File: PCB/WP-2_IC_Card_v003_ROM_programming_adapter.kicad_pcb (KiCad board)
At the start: 2 copper layers, 19.7 x 49.5 mm, 2 parts, among them J1 Conn_01x38_Male, J2 Conn_02x16_Counter_Clockwise

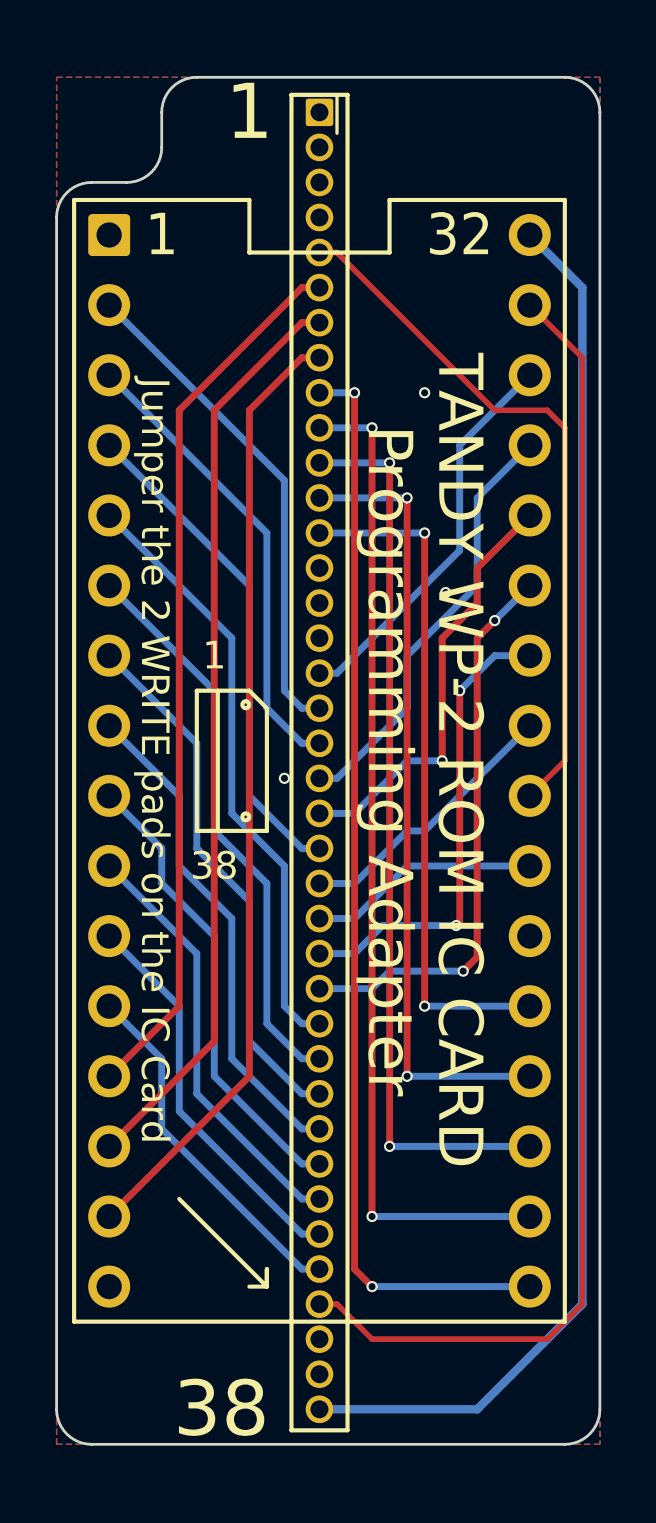
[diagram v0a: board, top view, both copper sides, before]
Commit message: reroute battery traces. cosmetics
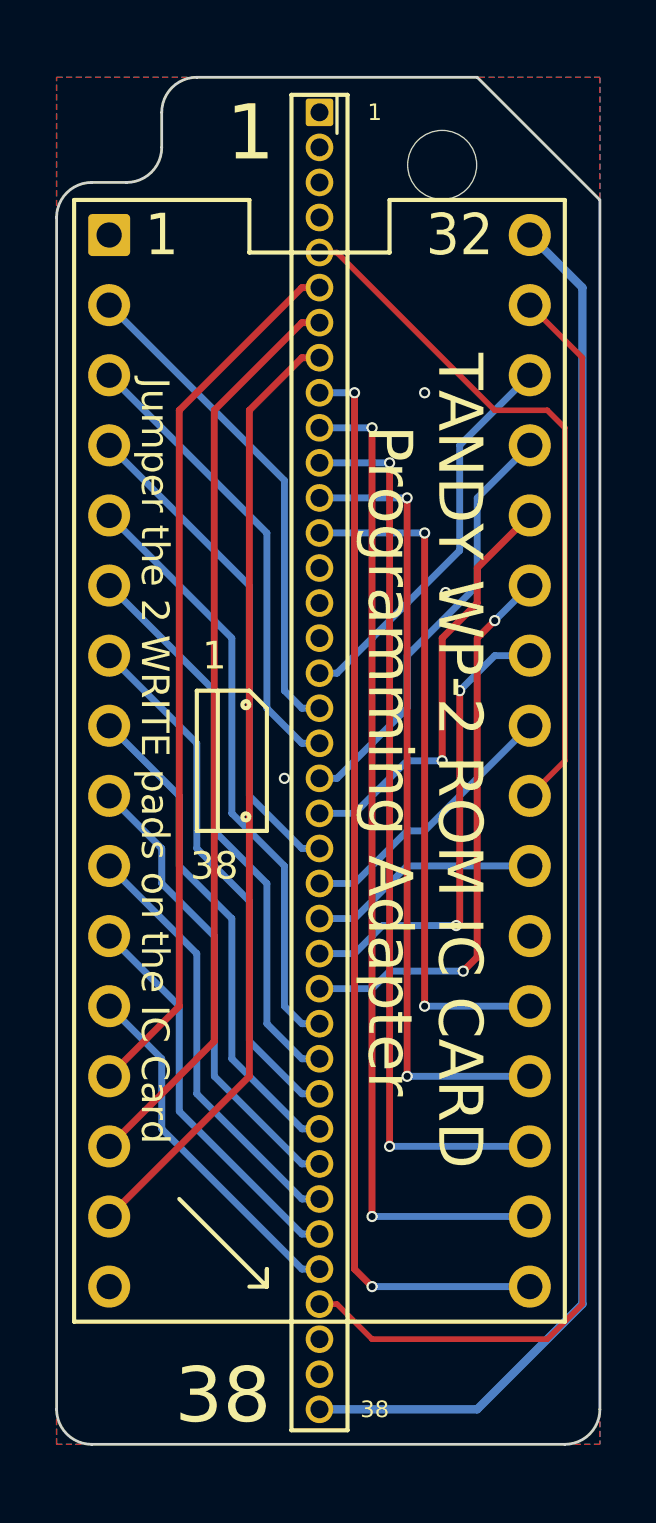
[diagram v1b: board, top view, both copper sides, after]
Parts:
- added REF**: MountingHole_2.5mm, MountingHole:MountingHole_2.5mm, F.Cu at (156.8, 80.0)
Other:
- outline, holes or cut-outs redrawn

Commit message: reduce programming adapter board size
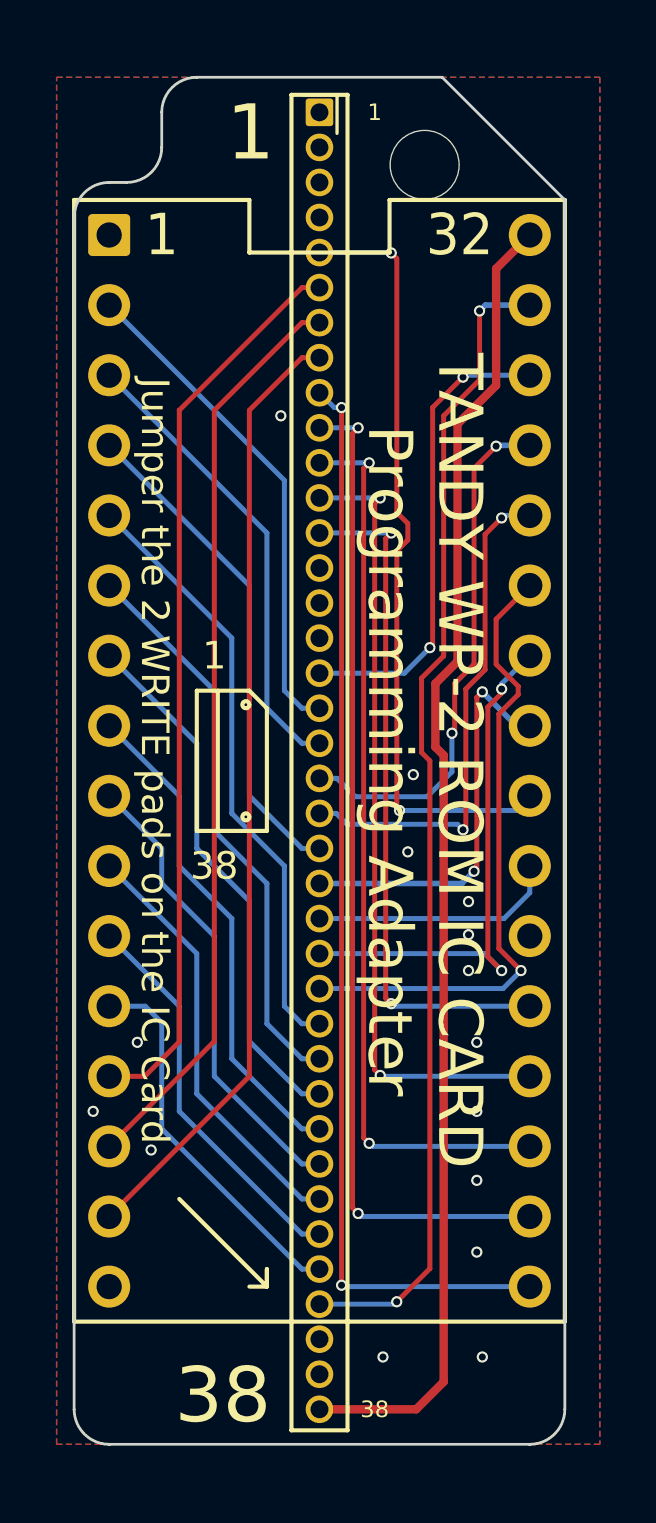
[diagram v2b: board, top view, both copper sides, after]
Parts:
- moved REF** 0.63 mm to (156.2, 80.0)
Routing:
- net /R~W: track 47.6 -> 42.1 mm, vias 0 -> 2
- net /A11: track 9.99 -> 15.3 mm, vias 0 -> 2
- net /A14: track 15.6 -> 19.1 mm, vias 0 -> 2
- net /A13: track 15.4 -> 18.4 mm, vias 1 -> 2
- net /A17: track 14.3 -> 17.2 mm, vias 0 -> 2
- net /~OE: track 25.4 -> 28.2 mm, vias 0 -> 2
- net /VDD: track 50.6 -> 48.0 mm
- net /A8: track 20.4 -> 23.0 mm, vias 2 -> 1
- net /A9: track 17.0 -> 19.1 mm
- net /A0: track 13.1 -> 13.8 mm
- net /D0: track 32.1 -> 32.9 mm
- net /A10: track 8.41 -> 8.98 mm
- net GND: vias 3 -> 15
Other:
- board size 19.7 x 49.5 mm -> 17.8 x 49.5 mm
- rule trace_min: 0.2 -> 0.16

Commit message: programming adapter routing
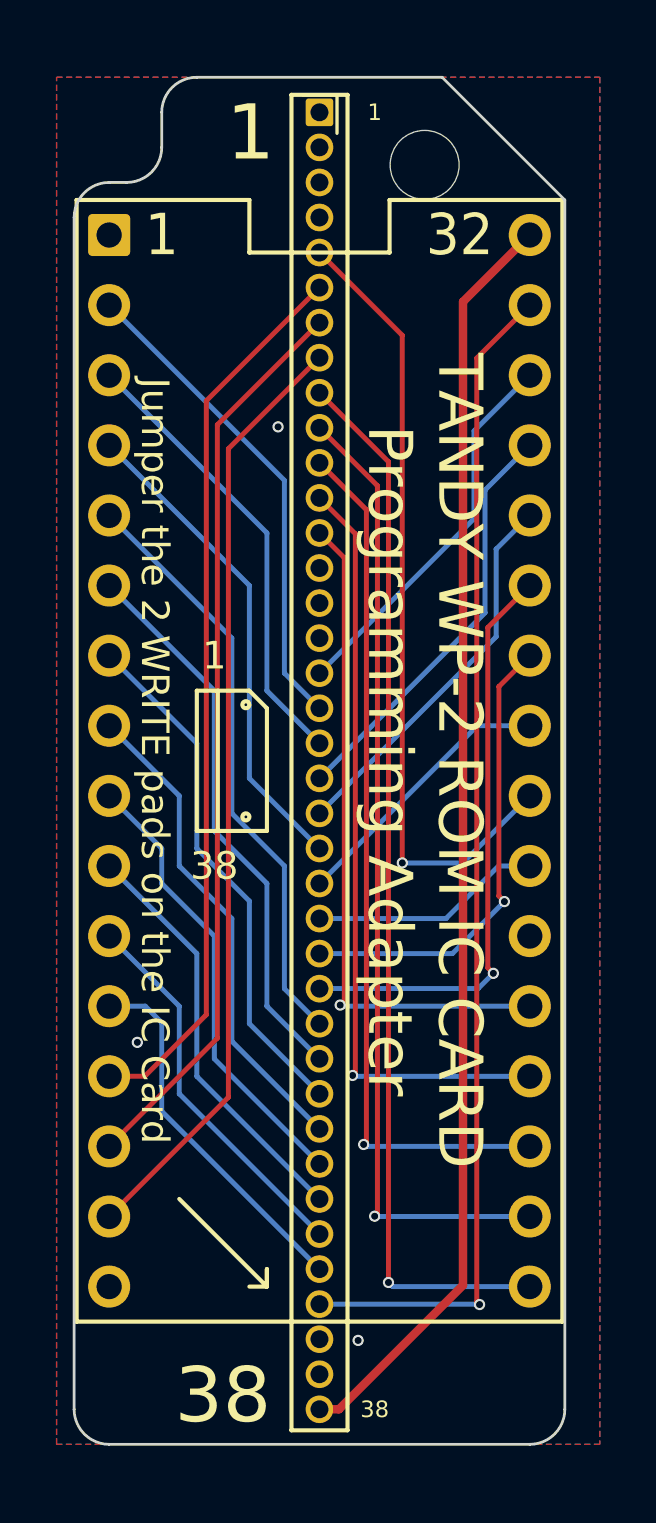
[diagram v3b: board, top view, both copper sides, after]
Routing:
- net /A11: track 15.3 -> 10.6 mm, vias 2 -> 0
- net /A13: track 18.4 -> 14.0 mm, vias 2 -> 0
- net /A14: track 19.1 -> 15.2 mm, vias 2 -> 0
- net /A17: track 17.2 -> 14.0 mm, vias 2 -> 0
- net /A9: track 19.1 -> 16.9 mm, vias 2 -> 1
- net /VDD: track 48.0 -> 46.1 mm
- net /A8: track 23.0 -> 21.3 mm
- net /D3: track 39.7 -> 38.5 mm, vias 2 -> 1
- net /D4: track 36.3 -> 35.1 mm, vias 2 -> 1
- net /D5: track 32.5 -> 31.5 mm, vias 2 -> 1
- net /D6: track 28.7 -> 27.9 mm, vias 2 -> 1
- net /~OE: track 28.2 -> 29.0 mm, vias 2 -> 1
- net /R~W: track 42.1 -> 42.9 mm, vias 2 -> 1
- net /A10: track 8.98 -> 8.41 mm
- net /D7: track 24.9 -> 24.4 mm, vias 2 -> 1
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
